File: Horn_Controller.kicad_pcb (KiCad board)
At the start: 4 copper layers, 99.8 x 95.2 mm, 132 parts, among them J1 RJ45, J2 MOLEX, J3 WAGO, J4 WAGO, J5 PHEONIX, K1 T9VV1K15, K2 T9VV1K15, Q1 BSS138, Q10 BSS138, Q11 BSS138, Q12 BSS138, Q13 BSS138, Q14 BSS138, Q15 BSS138, Q16 BSS138, Q17 BSS138, Q18 BSS138, Q19 BSS138, Q2 BSS138, Q20 BSS138, Q21 BSS138, Q22 BSS138, Q23 BSS138, Q24 BSS138, Q25 BSS138, Q26 BSS138, Q3 BSS138, Q4 BSS138, Q5 BSS138, Q6 BSS138, Q7 BSS138, Q8 BSS138, Q9 BSS138, U1 AP63205WU, U2 STM32F042G6Ux, U3 AP2112K-3.3, U4 ACS711, U5 ATA6561, U6 M24C02-FMC, U7 TCA6424A, Y1 32MHz

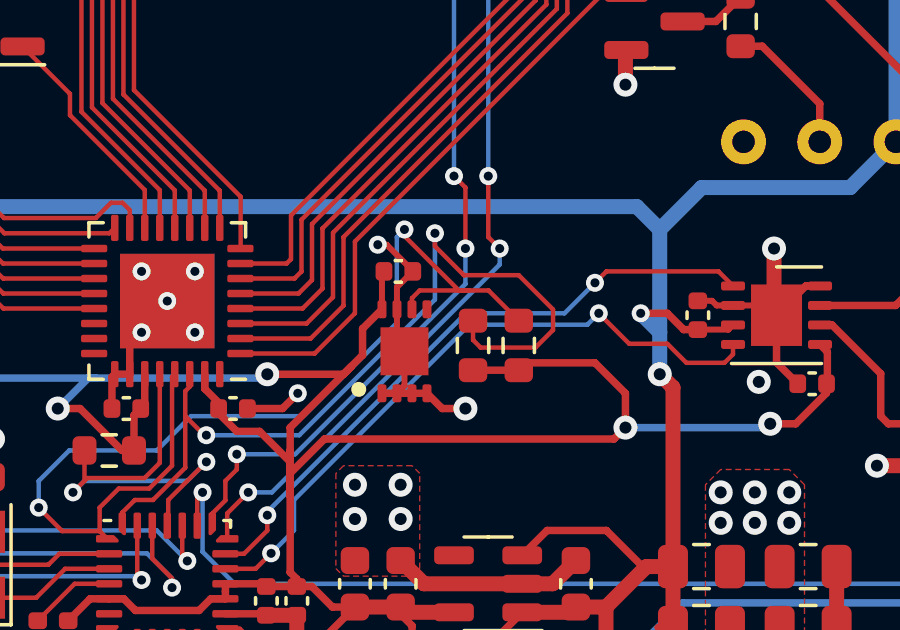
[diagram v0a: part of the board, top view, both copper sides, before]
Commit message: Added missing I2C trace
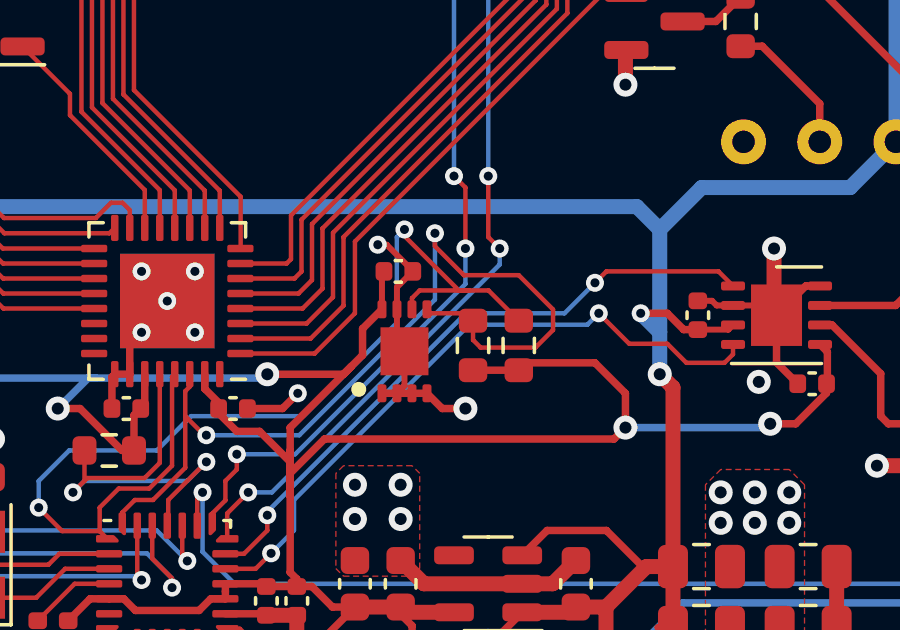
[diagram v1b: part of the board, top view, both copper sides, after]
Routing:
- net /SDA: track 28.5 -> 30.2 mm
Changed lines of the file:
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@@
   (segment (start 145.5715 92.456) (end 146.177 92.456) (width 0.15) (layer "F.Cu") (net 108))
   (segment (start 159.512 86.106) (end 159.512 86.789292) (width 0.15) (layer "F.Cu") (net 108))
+  (segment (start 155.309 86.1) (end 155.442 86.233) (width 0.15) (layer "F.Cu") (net 108))
   (segment (start 145.1525 93.2525) (end 145.1525 92.875) (width 0.15) (layer "F.Cu") (net 108))
   (segment (start 147.4025 88.67803) (end 147.4025 88.2615) (width 0.15) (layer "F.Cu") (net 108))
@@
   (segment (start 147.2525 89.662) (end 147.8875 90.297) (width 0.15) (layer "F.Cu") (net 108))
   (segment (start 155.575 83.998173) (end 156.539827 84.963) (width 0.15) (layer "F.Cu") (net 108))
+  (segment (start 155.442 86.233) (end 156.598 86.233) (width 0.15) (layer "F.Cu") (net 108))
   (segment (start 156.845 87.122) (end 156.845 86.48) (width 0.15) (layer "F.Cu") (net 108))
   (segment (start 155.575 83.566) (end 155.575 83.998173) (width 0.15) (layer "F.Cu") (net 108))
@@
   (segment (start 145.1525 92.875) (end 145.5715 92.456) (width 0.15) (layer "F.Cu") (net 108))
   (segment (start 146.177 92.456) (end 147.2525 91.3805) (width 0.15) (layer "F.Cu") (net 108))
+  (segment (start 156.598 86.233) (end 156.845 86.48) (width 0.15) (layer "F.Cu") (net 108))
   (via (at 155.575 83.566) (size 0.6) (drill 0.3) (layers "F.Cu" "B.Cu") (net 108))
   (via (at 147.955 90.297) (size 0.6) (drill 0.3) (layers "F.Cu" "B.Cu") (net 108))
